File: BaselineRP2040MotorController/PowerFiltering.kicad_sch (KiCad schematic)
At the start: 33 parts, among them U12 TLV1117LV33DCYR, U13 TX4139, U14 MT2492

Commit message: Erhhhhrh
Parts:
- removed C50: 1u, Capacitor_SMD:C_0603_1608Metric, symbol Device:C
- removed C53: 10u, Capacitor_SMD:C_0805_2012Metric, symbol Device:C
- removed C54, C63: 22uF 25V, Capacitor_SMD:C_0805_2012Metric, symbol Device:C
- removed C59: 22nF, Capacitor_SMD:C_0603_1608Metric, symbol Device:C
- removed C61: 22pF, Capacitor_SMD:C_0603_1608Metric, symbol Device:C
- removed C62: 47uF 10v, Capacitor_SMD:C_0805_2012Metric, symbol Device:C
- removed L2: 10uH, Inductor_SMD:L_Sunlord_SWPA5040S, symbol Device:L
- removed R60: 110k 0.1%, Resistor_SMD:R_0603_1608Metric, symbol Device:R
- removed R61: 15k 0.1%, Resistor_SMD:R_0603_1608Metric, symbol Device:R
- removed R62: 100k, Resistor_SMD:R_0603_1608Metric, symbol MotorController:TAYLOR_RESISTOR
- removed U12: TLV1117LV33DCYR, Package_TO_SOT_SMD:SOT-223-3_TabPin2, symbol Regulator_Linear:NCP1117-3.3_SOT223
- removed U14: MT2492, Package_TO_SOT_SMD:SOT-23-6, symbol Regulator_Switching:AP3211K
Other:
- note removed: "4.9-5.1V"

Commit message: Release for Review
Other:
- note removed: "10.5mm tall cap 11mm module stack height"
- note removed: "11.7-12.3V 2A"
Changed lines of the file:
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@@
 	(generator "eeschema")
 	(generator_version "8.0")
-	(paper "A4")
+	(paper "A5")
 	(junction
 		(at 161.29 60.96)
@@
 	(wire
 		(pts
-			(xy 38.1 48.26) (xy 43.18 48.26)
+			(xy 38.1 44.45) (xy 43.18 44.45)
 		)
 		(stroke
@@
 	(wire
 		(pts
-			(xy 38.1 76.2) (xy 43.18 76.2)
+			(xy 38.1 49.53) (xy 43.18 49.53)
 		)
 		(stroke
@@
 	(wire
 		(pts
-			(xy 43.18 76.2) (xy 43.18 77.47)
+			(xy 43.18 49.53) (xy 43.18 50.8)
 		)
 		(stroke
@@
 	(wire
 		(pts
-			(xy 38.1 30.48) (xy 43.18 30.48)
+			(xy 38.1 34.29) (xy 43.18 34.29)
 		)
 		(stroke
@@
 			(width 0)
 			(type default)
-		)
-	)
-	(arc
-		(start 73.66 74.93)
-		(mid 73.0324 70.7244)
-		(end 75.565 67.31)
-		(stroke
-			(width 0)
-			(type default)
-		)
-		(fill
-			(type none)
 		)
 	)
@@
 		)
 	)
-	(text "11.7-12.3V 2A"
-		(exclude_from_sim no)
-		(at 162.56 59.69 0)
-		(effects
-			(font
-				(size 0.6 0.6)
-			)
-			(justify left bottom)
-		)
-	)
 	(text "52 Volt input max"
 		(exclude_from_sim no)
@@
 			(font
 				(size 0.6 0.6)
-			)
-			(justify left bottom)
-		)
-	)
-	(text "10.5mm tall cap\n11mm module stack height"
-		(exclude_from_sim no)
-		(at 68.58 81.28 0)
-		(effects
-			(font
-				(size 2 2)
 			)
 			(justify left bottom)
@@
 	)
 	(label "VMOT_RAW"
-		(at 43.18 30.48 0)
+		(at 43.18 34.29 0)
 		(fields_autoplaced yes)
 		(effects
@@
 	(hierarchical_label "GND"
 		(shape bidirectional)
-		(at 38.1 76.2 180)
+		(at 38.1 49.53 180)
 		(fields_autoplaced yes)
 		(effects
@@
 	(hierarchical_label "VMOT_RAW"
 		(shape bidirectional)
-		(at 38.1 30.48 180)
+		(at 38.1 34.29 180)
 		(fields_autoplaced yes)
 		(effects
@@
 	(hierarchical_label "12V+"
 		(shape bidirectional)
-		(at 38.1 48.26 180)
+		(at 38.1 44.45 180)
 		(fields_autoplaced yes)
 		(effects
@@
 	(symbol
 		(lib_id "MotorBuck:VMOT")
-		(at 43.18 39.37 0)
+		(at 43.18 39.37 270)
 		(unit 1)
 		(exclude_from_sim no)
@@
 		(fields_autoplaced yes)
 		(property "Reference" "#PWR0123"
-			(at 43.18 43.18 0)
+			(at 39.37 39.37 0)
 			(effects
 				(font
@@
 		)
 		(property "Value" "VMOT"
-			(at 43.18 35.56 0)
-			(effects
-				(font
-					(size 1.27 1.27)
-				)
+			(at 46.99 39.3699 90)
+			(effects
+				(font
+					(size 1.27 1.27)
+				)
+				(justify left)
 			)
 		)
@@
 		)
 		(property "Sim.Device" "SPICE"
-			(at 43.18 43.18 0)
+			(at 39.37 39.37 0)
 			(effects
 				(font
@@
 		)
 		(property "Sim.Params" "type=\"I\" model=\"VMOT\" lib=\"\""
-			(at 1.905 -59.69 0)
+			(at 142.24 -1.905 0)
 			(effects
 				(font
@@
 		)
 		(property "Sim.Pins" "1=1"
-			(at 1.905 -59.69 0)
+			(at 142.24 -1.905 0)
 			(effects
 				(font
@@
 	(symbol
 		(lib_id "power:GND")
-		(at 43.18 77.47 0)
+		(at 43.18 50.8 0)
 		(unit 1)
 		(exclude_from_sim no)
@@
 		(dnp no)
 		(property "Reference" "#PWR0126"
-			(at 43.18 83.82 0)
+			(at 43.18 57.15 0)
 			(effects
 				(font
@@
 		)
 		(property "Value" "GND"
-			(at 43.307 81.8642 0)
+			(at 43.307 55.1942 0)
 			(effects
 				(font
@@
 		)
 		(property "Footprint" ""
-			(at 43.18 77.47 0)
+			(at 43.18 50.8 0)
 			(effects
 				(font
@@
 		)
 		(property "Datasheet" ""
-			(at 43.18 77.47 0)
+			(at 43.18 50.8 0)
 			(effects
 				(font
@@
 		)
 		(property "Description" ""
-			(at 43.18 77.47 0)
+			(at 43.18 50.8 0)
 			(effects
 				(font
@@
 	(symbol
 		(lib_id "power:+12V")
-		(at 43.18 48.26 0)
+		(at 43.18 44.45 270)
 		(unit 1)
 		(exclude_from_sim no)
@@
 		(fields_autoplaced yes)
 		(property "Reference" "#PWR0119"
-			(at 43.18 52.07 0)
+			(at 39.37 44.45 0)
 			(effects
 				(font
@@
 		)
 		(property "Value" "+12V"
-			(at 43.18 43.18 0)
-			(effects
-				(font
-					(size 1.27 1.27)
-				)
+			(at 46.99 44.4499 90)
+			(effects
+				(font
+					(size 1.27 1.27)
+				)
+				(justify left)
 			)
 		)
 		(property "Footprint" ""
-			(at 43.18 48.26 0)
+			(at 43.18 44.45 0)
 			(effects
 				(font
@@
 		)
 		(property "Datasheet" ""
-			(at 43.18 48.26 0)
+			(at 43.18 44.45 0)
 			(effects
 				(font
@@
 		)
 		(property "Description" ""
-			(at 43.18 48.26 0)
-			(effects
-				(font
+			(at 43.18 44.45 0)
+			(effects
+				(font

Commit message: Generate PDF
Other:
- title: (none) -> BLDC Starting Point
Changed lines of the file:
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@@
 	(generator_version "8.0")
 	(paper "A5")
+	(title_block
+		(title "BLDC Starting Point")
+		(comment 1 "Florian, Josh and EMF Group Release")
+	)
 	(junction
 		(at 161.29 60.96)

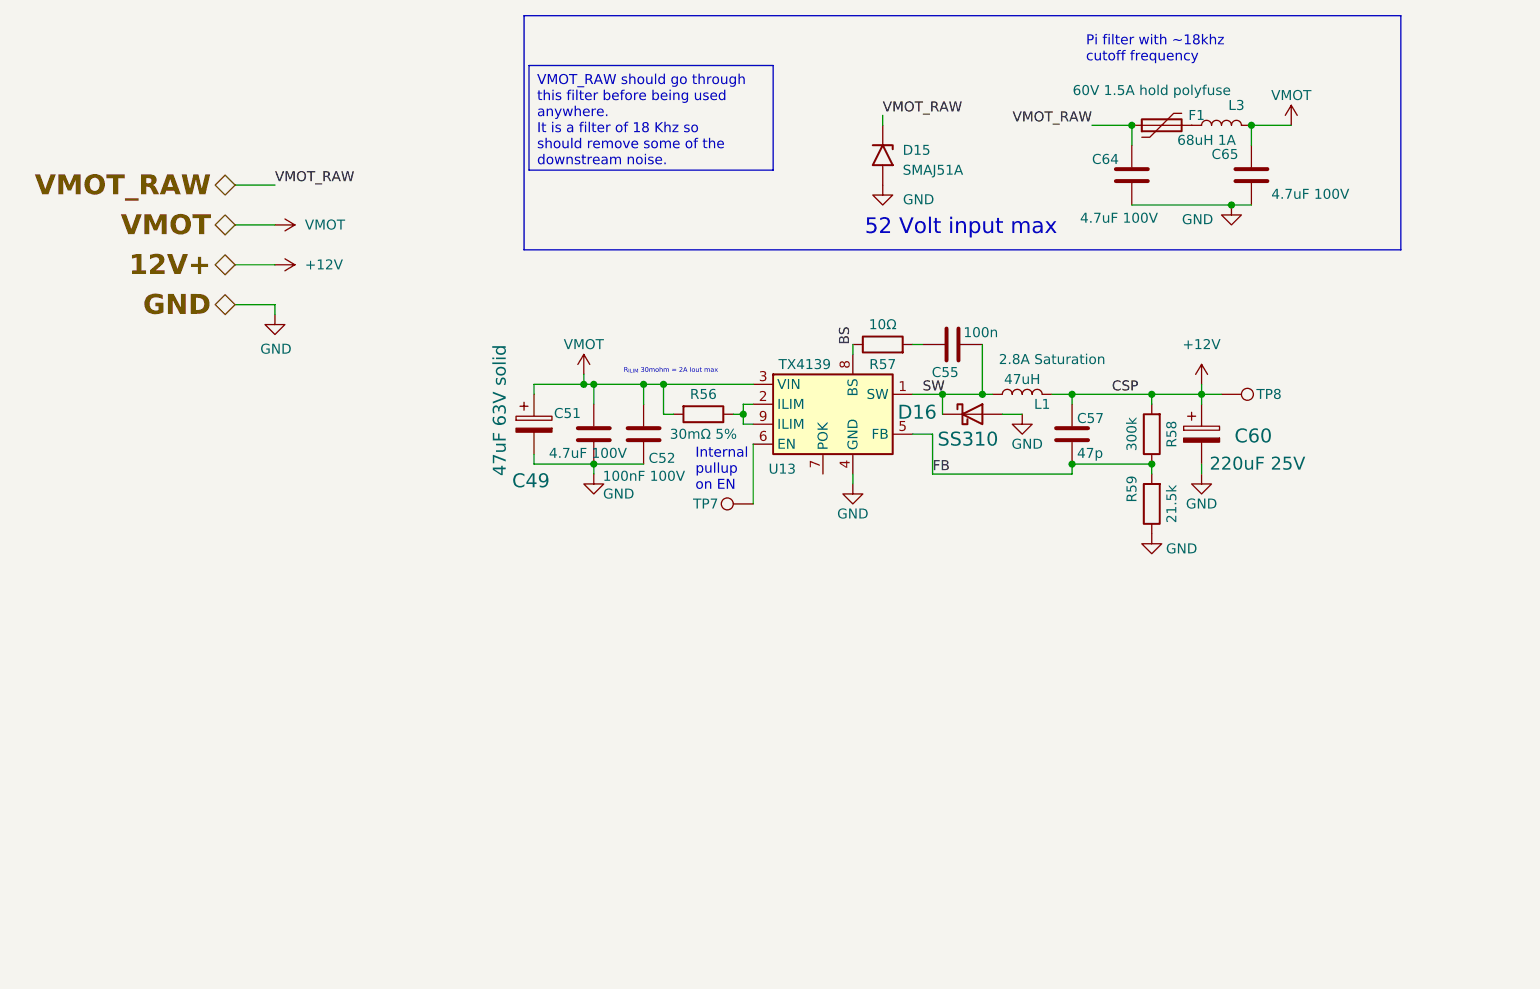
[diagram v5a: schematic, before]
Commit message: Should have been a 4 layer board.
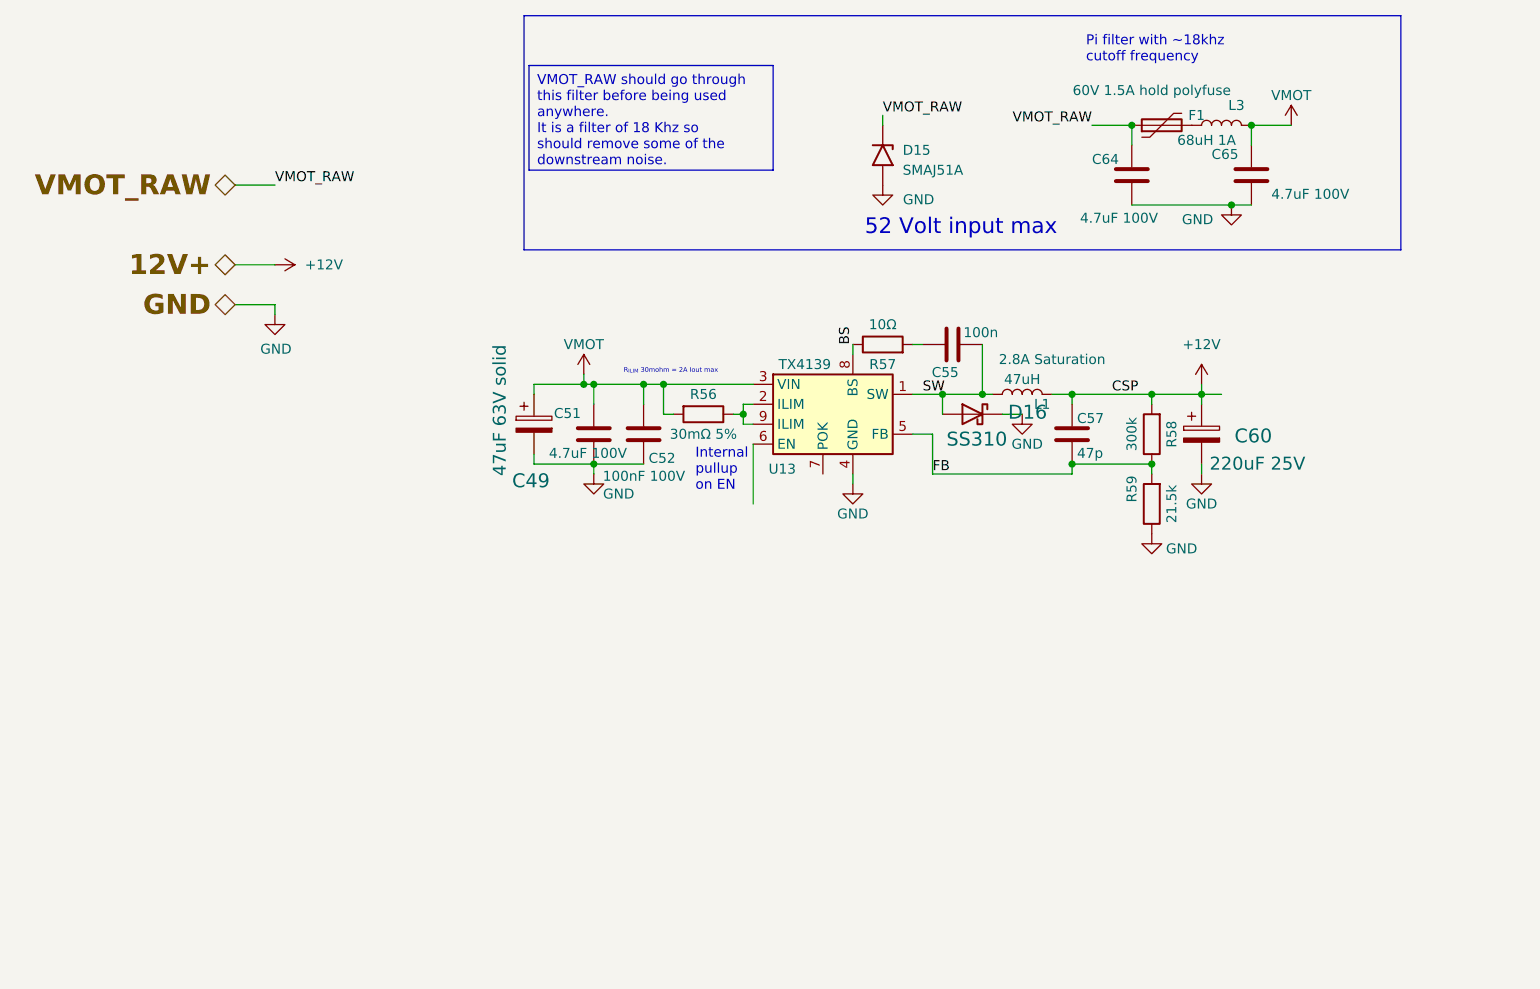
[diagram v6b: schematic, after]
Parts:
- removed TP7, TP8: TestPoint, TestPoint:TestPoint_Pad_D1.0mm, symbol Connector:TestPoint
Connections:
- net GND: now also D16.1 (K); no longer D16.2 (A)
- net SW: now also D16.2 (A); no longer D16.1 (K)

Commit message: Mounting points
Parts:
- added H1, H2, H3, H4: MountingHole_Pad, MountingHole:MountingHole_3.2mm_M3_DIN965_Pad_TopBottom, symbol Mechanical:MountingHole_Pad
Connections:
- net GND: now also H1.1, H2.1, H3.1, H4.1
